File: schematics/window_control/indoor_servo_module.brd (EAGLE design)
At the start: 48.2 x 59.4 mm, 29 parts, among them J1 MTR-SERVO-FS5103B, J2 JST-XH2.54-4P, J3 JST-XH2.54-2P, J4 JST-XH2.54-3P, Q2 2N3904, Q3 2N3906BU, Q4 2N3904, Q5 STP14NM50N, SW1 SWITCH, U2 LM311P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

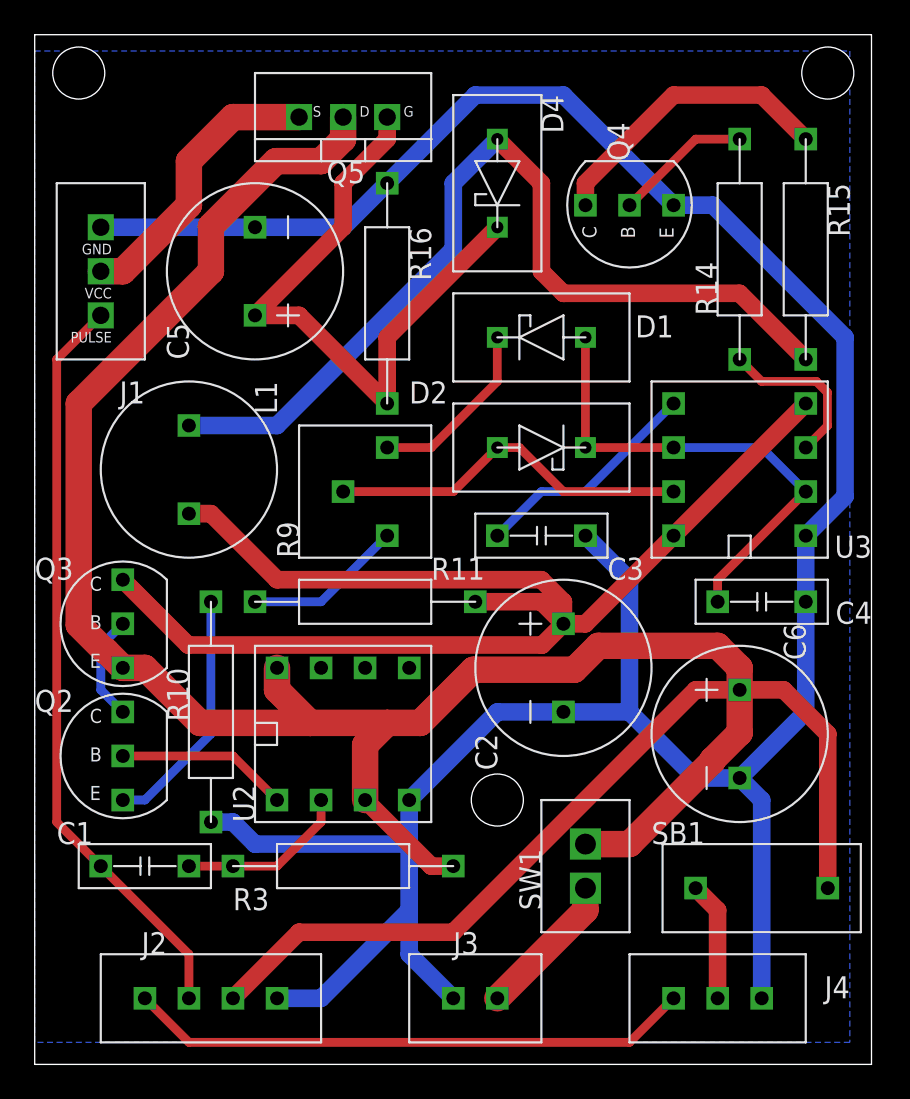
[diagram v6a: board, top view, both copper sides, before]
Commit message: Start preparing to order boards. Checked all labels
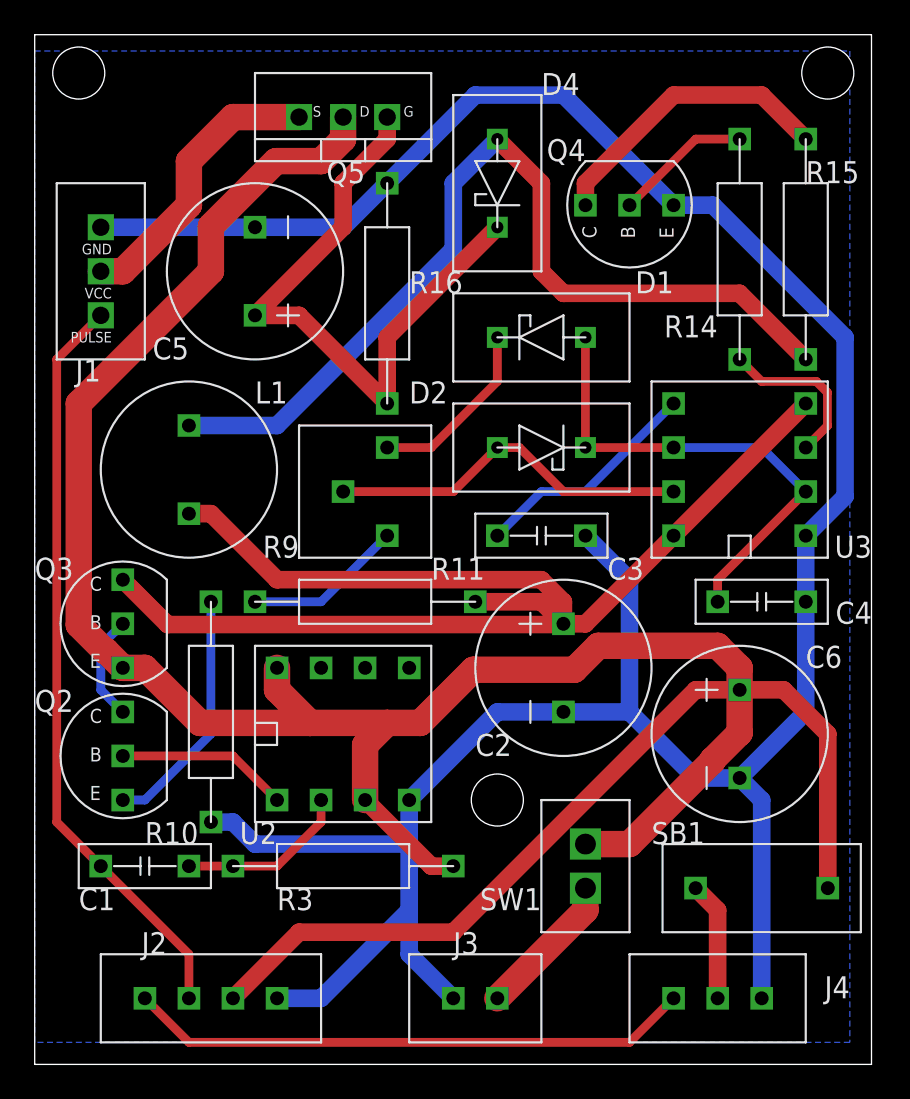
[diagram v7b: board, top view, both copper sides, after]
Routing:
- net +5V_IF_EN: track 77.3 -> 76.3 mm
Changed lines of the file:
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@@
 <elements>
 <element name="C1" library="my_devices" package="C-1" value="5nF" x="43.18" y="2.54" smashed="yes">
-<attribute name="NAME" x="38.1" y="3.81" size="1.27" layer="21"/>
+<attribute name="NAME" x="39.37" y="0" size="1.27" layer="21"/>
 </element>
 <element name="C2" library="my_devices" package="C" value="1000 uF" x="67.31" y="13.97" smashed="yes" rot="R270">
-<attribute name="NAME" x="62.23" y="10.16" size="1.27" layer="21" rot="R270"/>
+<attribute name="NAME" x="62.23" y="8.89" size="1.27" layer="21"/>
 </element>
 <element name="C3" library="my_devices" package="C-1" value="10 pF" x="66.04" y="21.59" smashed="yes">
@@
 </element>
 <element name="C5" library="my_devices" package="C" value="10 uF" x="49.53" y="36.83" smashed="yes" rot="R90">
-<attribute name="NAME" x="45.72" y="31.75" size="1.27" layer="21" rot="R90"/>
+<attribute name="NAME" x="45.72" y="33.02" size="1.27" layer="21" rot="R180"/>
 </element>
 <element name="D4" library="my_devices" package="D_SCHOTTKY" value="BAT41" x="63.5" y="41.91" smashed="yes" rot="R270">
-<attribute name="NAME" x="66.04" y="46.99" size="1.27" layer="21" rot="R270"/>
+<attribute name="NAME" x="66.04" y="46.99" size="1.27" layer="21"/>
 </element>
 <element name="J1" library="my_devices" package="SERVO" value="MTR-SERVO-FS5103B" x="40.64" y="36.83" smashed="yes" rot="R180">
-<attribute name="NAME" x="43.18" y="30.48" size="1.27" layer="21" rot="R180"/>
+<attribute name="NAME" x="40.64" y="31.75" size="1.27" layer="21" rot="R180"/>
 </element>
 <element name="L1" library="my_devices" package="L-RLB0914" value="RLB0914-102KL, 1000 uH" x="45.72" y="25.4" smashed="yes" rot="R270">
-<attribute name="NAME" x="49.53" y="30.48" size="1.27" layer="21" rot="R270"/>
+<attribute name="NAME" x="49.53" y="29.21" size="1.27" layer="21"/>
 </element>
 <element name="Q2" library="my_devices" package="TRANSISTOR" value="2N3904" x="40.64" y="7.62" smashed="yes">
@@
 </element>
 <element name="Q4" library="my_devices" package="TRANSISTOR" value="2N3904" x="72.39" y="39.37" smashed="yes" rot="R90">
-<attribute name="NAME" x="71.12" y="43.18" size="1.27" layer="21" rot="R90"/>
+<attribute name="NAME" x="68.58" y="44.45" size="1.27" layer="21" rot="R180"/>
 </element>
 <element name="Q5" library="my_devices" package="MOSFET_N" value="STP14NM50N" x="54.61" y="45.72" smashed="yes" rot="R180">
@@
 </element>
 <element name="R10" library="my_devices" package="R" value="200" x="46.99" y="11.43" smashed="yes" rot="R270">
-<attribute name="NAME" x="44.45" y="13.97" size="1.27" layer="21" rot="R270"/>
+<attribute name="NAME" x="43.18" y="3.81" size="1.27" layer="21"/>
 <attribute name="R" value="" x="-5.08" y="-24.13" size="1.778" layer="27" rot="R270" display="off"/>
 </element>
@@
 </element>
 <element name="R14" library="my_devices" package="R" value="100" x="77.47" y="38.1" smashed="yes" rot="R90">
-<attribute name="NAME" x="76.2" y="34.29" size="1.27" layer="21" rot="R90"/>
+<attribute name="NAME" x="76.2" y="34.29" size="1.27" layer="21" rot="R180"/>
 <attribute name="R" value="" x="133.35" y="58.42" size="1.778" layer="27" rot="R90" display="off"/>
 </element>
 <element name="R15" library="my_devices" package="R" value="5" x="81.28" y="38.1" smashed="yes" rot="R270">
-<attribute name="NAME" x="82.55" y="41.91" size="1.27" layer="21" rot="R270"/>
+<attribute name="NAME" x="81.28" y="41.91" size="1.27" layer="21"/>
 <attribute name="R" value="" x="25.4" y="2.54" size="1.778" layer="27" rot="R270" display="off"/>
 </element>
 <element name="R16" library="my_devices" package="R" value="3K" x="57.15" y="35.56" smashed="yes" rot="R270">
-<attribute name="NAME" x="58.42" y="39.37" size="1.27" layer="21" rot="R270"/>
+<attribute name="NAME" x="58.42" y="35.56" size="1.27" layer="21"/>
 <attribute name="R" value="" x="1.27" y="-15.24" size="1.778" layer="27" rot="R270" display="off"/>
 </element>
 <element name="R3" library="my_devices" package="R" value="150K" x="54.61" y="2.54" smashed="yes">
-<attribute name="NAME" x="48.26" y="0" size="1.27" layer="21"/>
+<attribute name="NAME" x="50.8" y="0" size="1.27" layer="21"/>
 <attribute name="R" value="" x="74.93" y="-49.53" size="1.778" layer="27" display="off"/>
 </element>
 <element name="R9" library="my_devices" package="RD-3362H" value="20K" x="55.88" y="24.13" smashed="yes" rot="R90">
-<attribute name="NAME" x="52.07" y="20.32" size="1.27" layer="21" rot="R90"/>
+<attribute name="NAME" x="52.07" y="21.59" size="1.27" layer="21" rot="R180"/>
 </element>
 <element name="SB1" library="my_devices" package="SB-NC" value="KLS7-DS-01-B-00" x="78.74" y="1.27" smashed="yes">
@@
 </element>
 <element name="SW1" library="my_devices" package="SWITCH" value="SWITCH" x="68.58" y="2.54" smashed="yes" rot="R90">
-<attribute name="NAME" x="66.04" y="0" size="1.27" layer="21" rot="R90"/>
+<attribute name="NAME" x="66.04" y="1.27" size="1.27" layer="21" rot="R180"/>
 </element>
 <element name="U2" library="my_devices" package="DIP8" value="LM311P" x="54.61" y="10.16" smashed="yes" rot="R90">
-<attribute name="NAME" x="49.53" y="5.08" size="1.27" layer="21" rot="R90"/>
+<attribute name="NAME" x="50.8" y="5.08" size="1.27" layer="21" rot="R180"/>
 </element>
 <element name="U3" library="my_devices" package="DIP8" value="NE555P" x="77.47" y="25.4" smashed="yes" rot="R180">
@@
 </element>
 <element name="C6" library="my_devices" package="C" value="1000 uF" x="77.47" y="10.16" smashed="yes" rot="R270">
-<attribute name="NAME" x="80.01" y="16.51" size="1.27" layer="21" rot="R270"/>
+<attribute name="NAME" x="81.28" y="13.97" size="1.27" layer="21"/>
 </element>
 <element name="D1" library="my_devices" package="D_SCHOTTKY" value="BAT41" x="66.04" y="33.02" smashed="yes" rot="R180">
-<attribute name="NAME" x="73.66" y="34.29" size="1.27" layer="21" rot="R180"/>
+<attribute name="NAME" x="73.66" y="36.83" size="1.27" layer="21" rot="R180"/>
 </element>
 <element name="D2" library="my_devices" package="D_SCHOTTKY" value="BAT41" x="66.04" y="26.67" smashed="yes">
@@
 <wire x1="68.58" y1="16.51" x2="67.31" y2="16.51" width="1.016" layer="1"/>
 <wire x1="67.2656" y1="16.4656" x2="67.31" y2="16.51" width="1.016" layer="1"/>
-<wire x1="41.91" y1="19.05" x2="45.6756" y2="15.2844" width="1.016" layer="1"/>
-<wire x1="66.0844" y1="15.2844" x2="67.31" y2="16.51" width="1.016" layer="1"/>
-<wire x1="45.6756" y1="15.2844" x2="66.0844" y2="15.2844" width="1.016" layer="1"/>
 <wire x1="67.31" y1="16.51" x2="67.31" y2="17.78" width="1.016" layer="1"/>
 <wire x1="67.31" y1="17.78" x2="66.04" y2="19.05" width="1.016" layer="1"/>
@@
 <wire x1="46.99" y1="22.86" x2="45.72" y2="22.86" width="1.016" layer="1"/>
 <wire x1="66.04" y1="19.05" x2="50.8" y2="19.05" width="1.016" layer="1"/>
+<wire x1="41.91" y1="19.05" x2="44.4944" y2="16.4656" width="1.016" layer="1"/>
+<wire x1="44.4944" y1="16.4656" x2="67.2656" y2="16.4656" width="1.016" layer="1"/>
 </signal>
 <signal name="N$35">

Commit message: Boards checked and ready to order
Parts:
- moved D1 1.27 mm to (66.0, 31.8)
- moved D4 1.27 mm to (63.5, 40.6)
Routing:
- net N$48: track 10.5 -> 7.93 mm
- net N$51: track 37.1 -> 34.6 mm
- net N$46: track 28.6 -> 26.0 mm
- net N$39: track 52.9 -> 50.6 mm
- net N$44: track 13.3 -> 14.1 mm
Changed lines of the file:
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@@
 <drawing>
 <settings>
-<setting alwaysvectorfont="yes"/>
+<setting alwaysvectorfont="no"/>
 <setting verticaltext="up"/>
 </settings>
@@
 <attribute name="NAME" x="45.72" y="33.02" size="1.27" layer="21" rot="R180"/>
 </element>
-<element name="D4" library="my_devices" package="D_SCHOTTKY" value="BAT41" x="63.5" y="41.91" smashed="yes" rot="R270">
-<attribute name="NAME" x="66.04" y="46.99" size="1.27" layer="21"/>
+<element name="D4" library="my_devices" package="D_SCHOTTKY" value="BAT41" x="63.5" y="40.64" smashed="yes" rot="R270">
+<attribute name="NAME" x="62.23" y="46.99" size="1.27" layer="21"/>
 </element>
 <element name="J1" library="my_devices" package="SERVO" value="MTR-SERVO-FS5103B" x="40.64" y="36.83" smashed="yes" rot="R180">
@@
 <attribute name="NAME" x="81.28" y="13.97" size="1.27" layer="21"/>
 </element>
-<element name="D1" library="my_devices" package="D_SCHOTTKY" value="BAT41" x="66.04" y="33.02" smashed="yes" rot="R180">
-<attribute name="NAME" x="73.66" y="36.83" size="1.27" layer="21" rot="R180"/>
+<element name="D1" library="my_devices" package="D_SCHOTTKY" value="BAT41" x="66.04" y="31.75" smashed="yes" rot="R180">
+<attribute name="NAME" x="73.66" y="35.56" size="1.27" layer="21" rot="R180"/>
 </element>
 <element name="D2" library="my_devices" package="D_SCHOTTKY" value="BAT41" x="66.04" y="26.67" smashed="yes">
@@
 <contactref element="L1" pad="P$2"/>
 <contactref element="R15" pad="P$2"/>
-<wire x1="67.31" y1="35.56" x2="66.04" y2="36.83" width="1.016" layer="1"/>
-<wire x1="77.47" y1="35.56" x2="81.28" y2="31.75" width="1.016" layer="1"/>
-<wire x1="67.31" y1="35.56" x2="77.47" y2="35.56" width="1.016" layer="1"/>
 <wire x1="45.72" y1="27.94" x2="50.8" y2="27.94" width="1.016" layer="16"/>
-<wire x1="66.04" y1="41.91" x2="63.5" y2="44.45" width="1.016" layer="1"/>
-<wire x1="66.04" y1="36.83" x2="66.04" y2="41.91" width="1.016" layer="1"/>
-<wire x1="60.96" y1="38.1" x2="60.96" y2="41.91" width="1.016" layer="16"/>
-<wire x1="60.96" y1="41.91" x2="63.5" y2="44.45" width="1.016" layer="16"/>
-<wire x1="50.8" y1="27.94" x2="60.96" y2="38.1" width="1.016" layer="16"/>
+<wire x1="74.93" y1="38.1" x2="68.58" y2="38.1" width="1.016" layer="1"/>
+<wire x1="68.58" y1="38.1" x2="63.5" y2="43.18" width="1.016" layer="1"/>
+<wire x1="63.5" y1="43.18" x2="63.5" y2="44.45" width="1.016" layer="1"/>
+<wire x1="81.28" y1="31.75" x2="74.93" y2="38.1" width="1.016" layer="1"/>
+<wire x1="63.5" y1="40.64" x2="63.5" y2="44.45" width="1.016" layer="16"/>
+<wire x1="50.8" y1="27.94" x2="63.5" y2="40.64" width="1.016" layer="16"/>
 </signal>
 <signal name="N$40">
@@
 <contactref element="U3" pad="PIN_5"/>
 <contactref element="C3" pad="P$1"/>
-<wire x1="71.12" y1="26.67" x2="73.66" y2="29.21" width="0.508" layer="16"/>
 <wire x1="63.5" y1="21.59" x2="66.04" y2="24.13" width="0.508" layer="16"/>
-<wire x1="66.04" y1="24.13" x2="68.58" y2="24.13" width="0.508" layer="16"/>
-<wire x1="68.58" y1="24.13" x2="71.12" y2="26.67" width="0.508" layer="16"/>
+<wire x1="69.85" y1="24.13" x2="72.39" y2="26.67" width="0.508" layer="16"/>
+<wire x1="72.39" y1="26.67" x2="72.39" y2="27.94" width="0.508" layer="16"/>
+<wire x1="72.39" y1="27.94" x2="73.66" y2="29.21" width="0.508" layer="16"/>
+<wire x1="66.04" y1="24.13" x2="69.85" y2="24.13" width="0.508" layer="16"/>
 </signal>
 <signal name="N$46">
@@
 <wire x1="76.2" y1="17.78" x2="76.2" y2="19.05" width="0.508" layer="1"/>
 <wire x1="76.2" y1="19.05" x2="81.28" y2="24.13" width="0.508" layer="1"/>
-<wire x1="68.58" y1="33.02" x2="68.58" y2="26.67" width="0.508" layer="1"/>
-<wire x1="68.58" y1="26.67" x2="73.66" y2="26.67" width="0.508" layer="1"/>
 <wire x1="73.66" y1="26.67" x2="78.74" y2="26.67" width="0.508" layer="16"/>
 <wire x1="78.74" y1="26.67" x2="81.28" y2="24.13" width="0.508" layer="16"/>
+<wire x1="69.85" y1="31.75" x2="69.85" y2="26.67" width="0.508" layer="1"/>
+<wire x1="69.85" y1="26.67" x2="73.66" y2="26.67" width="0.508" layer="1"/>
 </signal>
 <signal name="N$47">
@@
 <contactref element="R9" pad="P3"/>
 <contactref element="D2" pad="ANODE"/>
-<wire x1="60.96" y1="24.13" x2="63.5" y2="26.67" width="0.508" layer="1"/>
-<wire x1="54.61" y1="24.13" x2="60.96" y2="24.13" width="0.508" layer="1"/>
-<wire x1="63.5" y1="26.67" x2="64.77" y2="26.67" width="0.508" layer="1"/>
-<wire x1="64.77" y1="26.67" x2="67.31" y2="24.13" width="0.508" layer="1"/>
-<wire x1="67.31" y1="24.13" x2="73.66" y2="24.13" width="0.508" layer="1"/>
+<wire x1="59.69" y1="24.13" x2="62.23" y2="26.67" width="0.508" layer="1"/>
+<wire x1="54.61" y1="24.13" x2="59.69" y2="24.13" width="0.508" layer="1"/>
+<wire x1="62.23" y1="26.67" x2="64.77" y2="24.13" width="0.508" layer="1"/>
+<wire x1="64.77" y1="24.13" x2="73.66" y2="24.13" width="0.508" layer="1"/>
 </signal>
 <signal name="N$48">
 <contactref element="R9" pad="P2"/>
 <contactref element="D1" pad="CATHODE"/>
-<wire x1="57.15" y1="26.67" x2="59.69" y2="26.67" width="0.508" layer="1"/>
-<wire x1="59.69" y1="26.67" x2="63.5" y2="30.48" width="0.508" layer="1"/>
-<wire x1="63.5" y1="30.48" x2="63.5" y2="33.02" width="0.508" layer="1"/>
+<wire x1="57.15" y1="26.67" x2="58.42" y2="26.67" width="0.508" layer="1"/>
+<wire x1="58.42" y1="26.67" x2="62.23" y2="30.48" width="0.508" layer="1"/>
+<wire x1="62.23" y1="30.48" x2="62.23" y2="31.75" width="0.508" layer="1"/>
 </signal>
 <signal name="N$49">
@@
 <wire x1="57.15" y1="44.45" x2="57.15" y2="45.72" width="1.016" layer="1"/>
 <wire x1="54.61" y1="41.91" x2="57.15" y2="44.45" width="1.016" layer="1"/>
-<wire x1="57.15" y1="29.21" x2="57.15" y2="33.02" width="1.016" layer="1"/>
-<wire x1="57.15" y1="33.02" x2="63.5" y2="39.37" width="1.016" layer="1"/>
+<wire x1="57.15" y1="29.21" x2="63.5" y2="35.56" width="1.016" layer="1"/>
+<wire x1="63.5" y1="35.56" x2="63.5" y2="36.83" width="1.016" layer="1"/>
 </signal>
 <signal name="N$37">
